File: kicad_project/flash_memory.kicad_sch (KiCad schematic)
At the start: 4 parts, among them U1 W25Q128JVSIQ

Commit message: Pcb to production
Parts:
- removed TP6: VDD_SPI, TestPoint:TestPoint_Pad_D1.0mm, symbol Connector:TestPoint
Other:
- note added: "FLASH MEMORY"
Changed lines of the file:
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@@
 	(title_block
 		(title "WebScreen Project")
-		(rev "0")
+		(date "2024-11-02")
+		(rev "1.2")
 		(company "HW Media Lab LLC")
 	)
@@
 		(color 0 0 0 0)
 	)
-	(junction
-		(at 138.43 95.25)
-		(diameter 0)
-		(color 0 0 0 0)
-	)
 	(wire
 		(pts
@@
 	(wire
 		(pts
-			(xy 138.43 95.25) (xy 152.4 95.25)
-		)
-		(stroke
-			(width 0)
-			(type default)
-		)
-	)
-	(wire
-		(pts
 			(xy 166.37 97.79) (xy 166.37 105.41)
 		)
@@
 	(wire
 		(pts
-			(xy 125.73 95.25) (xy 138.43 95.25)
+			(xy 125.73 95.25) (xy 152.4 95.25)
 		)
 		(stroke
@@
 			(width 0)
 			(type default)
+		)
+	)
+	(text "FLASH MEMORY"
+		(exclude_from_sim no)
+		(at 208.534 28.956 0)
+		(effects
+			(font
+				(face "ISOCPEUR")
+				(size 7.62 7.62)
+				(thickness 0.254)
+				(bold yes)
+			)
+			(justify left bottom)
 		)
 	)
@@
 		(shape output)
 		(at 182.88 113.03 0)
-		(fields_autoplaced yes)
 		(effects
 			(font
@@
 		(shape output)
 		(at 182.88 110.49 0)
-		(fields_autoplaced yes)
 		(effects
 			(font
@@
 		(shape output)
 		(at 182.88 118.11 0)
-		(fields_autoplaced yes)
 		(effects
 			(font
@@
 		(shape output)
 		(at 182.88 97.79 0)
-		(fields_autoplaced yes)
 		(effects
 			(font
@@
 		(shape output)
 		(at 182.88 115.57 0)
-		(fields_autoplaced yes)
 		(effects
 			(font
@@
 		(shape output)
 		(at 182.88 107.95 0)
-		(fields_autoplaced yes)
 		(effects
 			(font
@@
 		(shape output)
 		(at 182.88 105.41 0)
-		(fields_autoplaced yes)
 		(effects
 			(font
@@
 			)
 			(justify left)
-		)
-	)
-	(symbol
-		(lib_id "Connector:TestPoint")
-		(at 138.43 95.25 0)
-		(unit 1)
-		(exclude_from_sim no)
-		(in_bom no)
-		(on_board yes)
-		(dnp yes)
-		(fields_autoplaced yes)
-		(property "Reference" "TP6"
-			(at 139.827 90.7359 0)
-			(effects
-				(font
-					(size 1.27 1.27)
-				)
-				(justify left)
-			)
-		)
-		(property "Value" "VDD_SPI"
-			(at 139.827 93.1601 0)
-			(effects
-				(font
-					(size 1.27 1.27)
-				)
-				(justify left)
-			)
-		)
-		(property "Footprint" "TestPoint:TestPoint_Pad_D1.0mm"
-			(at 143.51 95.25 0)
-			(effects
-				(font
-					(size 1.27 1.27)
-				)
-				(hide yes)
-			)
-		)
-		(property "Datasheet" "~"
-			(at 143.51 95.25 0)
-			(effects
-				(font
-					(size 1.27 1.27)
-				)
-				(hide yes)
-			)
-		)
-		(property "Description" ""
-			(at 138.43 95.25 0)
-			(effects
-				(font
-					(size 1.27 1.27)
-				)
-				(hide yes)
-			)
-		)
-		(property "MFN" ""
-			(at 138.43 95.25 0)
-			(effects
-				(font
-					(size 1.27 1.27)
-				)
-				(hide yes)
-			)
-		)
-		(pin "1"
-		)
-		(instances
-			(project "Display_pcb"
-				(path "/b5a94c04-25f7-450f-b87b-275489bc56c3/8e85ac6e-1427-45a0-aa64-3ffb0278b793"
-					(reference "TP6")
-					(unit 1)
-				)
-			)
 		)
 	)
@@
 			)
 		)
+		(property "Sim.Device" ""
+			(at 152.4 113.03 0)
+			(effects
+				(font
+					(size 1.27 1.27)
+				)
+				(hide yes)
+			)
+		)
+		(property "Sim.Pins" ""
+			(at 152.4 113.03 0)
+			(effects
+				(font
+					(size 1.27 1.27)
+				)
+				(hide yes)
+			)
+		)
 		(pin "1"
 		)
@@
 			)
 		)
+		(property "Sim.Device" ""
+			(at 125.73 100.33 0)
+			(effects
+				(font
+					(size 1.27 1.27)
+				)
+				(hide yes)
+			)
+		)
+		(property "Sim.Pins" ""
+			(at 125.73 100.33 0)
+			(effects
+				(font
+					(size 1.27 1.27)
+				)
+				(hide yes)
+			)
+		)
 		(pin "1"
 		)
@@
 			(at 173.99 97.79 0)
 			(effects
+				(font
+					(size 1.27 1.27)
+				)
+				(hide yes)
+			)
+		)
+		(property "Sim.Device" ""
+			(at 173.99 97.79 0)
+			(effects
+				(font
+					(size 1.27 1.27)
+				)
+				(hide yes)
+			)
+		)
+		(property "Sim.Pins" ""
+			(at 173.99 97.79 0)
+			(effects

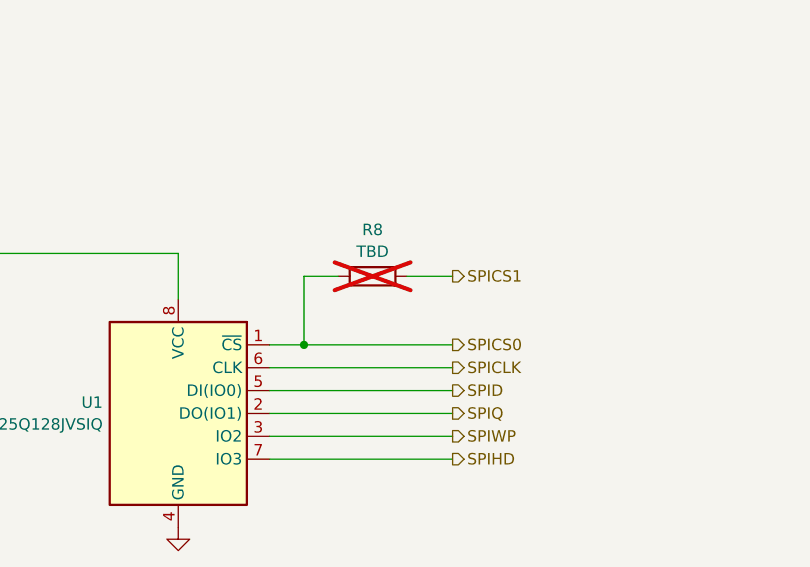
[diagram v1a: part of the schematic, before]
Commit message: Design revision: SD improvements, flash update, silkscreen and USB differential fix
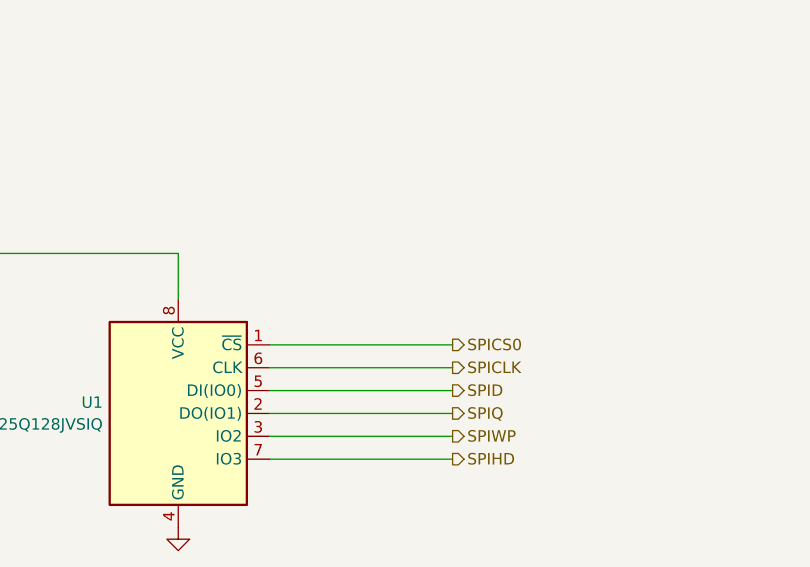
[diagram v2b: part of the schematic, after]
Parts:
- removed R8: TBD, Resistor_SMD:R_0402_1005Metric, symbol Device:R
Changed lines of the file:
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@@
-	)
-	(junction
-		(at 166.37 105.41)
-		(diameter 0)
-		(color 0 0 0 0)
 	)
 	(junction
@@
 	(wire
 		(pts
-			(xy 166.37 105.41) (xy 182.88 105.41)
+			(xy 162.56 105.41) (xy 182.88 105.41)
 		)
 		(stroke
@@
 	(wire
 		(pts
-			(xy 177.8 97.79) (xy 182.88 97.79)
-		)
-		(stroke
-			(width 0)
-			(type default)
-		)
-	)
-	(wire
-		(pts
-			(xy 162.56 105.41) (xy 166.37 105.41)
-		)
-		(stroke
-			(width 0)
-			(type default)
-		)
-	)
-	(wire
-		(pts
-			(xy 166.37 97.79) (xy 166.37 105.41)
-		)
-		(stroke
-			(width 0)
-			(type default)
-		)
-	)
-	(wire
-		(pts
 			(xy 125.73 92.71) (xy 125.73 95.25)
 		)
@@
 		(pts
 			(xy 125.73 95.25) (xy 152.4 95.25)
-		)
-		(stroke
-			(width 0)
-			(type default)
-		)
-	)
-	(wire
-		(pts
-			(xy 170.18 97.79) (xy 166.37 97.79)
 		)
 		(stroke
@@
 		(shape output)
 		(at 182.88 118.11 0)
-		(effects
-			(font
-				(size 1.27 1.27)
-			)
-			(justify left)
-		)
-	)
-	(hierarchical_label "SPICS1"
-		(shape output)
-		(at 182.88 97.79 0)
 		(effects
 			(font
@@
 					(unit 1)
 				)
-			)
-		)
-	)
-	(symbol
-		(lib_id "Device:R")
-		(at 173.99 97.79 90)
-		(unit 1)
-		(exclude_from_sim no)
-		(in_bom no)
-		(on_board yes)
-		(dnp yes)
-		(property "Reference" "R8"
-			(at 173.99 92.6297 90)
-			(effects
-				(font
-					(size 1.27 1.27)
-				)
-			)
-		)
-		(property "Value" "TBD"
-			(at 173.99 95.0539 90)
-			(effects
-				(font
-					(size 1.27 1.27)
-				)
-			)
-		)
-		(property "Footprint" "Resistor_SMD:R_0402_1005Metric"
-			(at 173.99 99.568 90)
-			(effects
-				(font
-					(size 1.27 1.27)
-				)
-				(hide yes)
-			)
-		)
-		(property "Datasheet" "~"
-			(at 173.99 97.79 0)
-			(effects
-				(font
-					(size 1.27 1.27)
-				)
-				(hide yes)
-			)
-		)
-		(property "Description" ""
-			(at 173.99 97.79 0)
-			(effects
-				(font
-					(size 1.27 1.27)
-				)
-				(hide yes)
-			)
-		)
-		(property "MFN" ""
-			(at 173.99 97.79 0)
-			(effects
-				(font
-					(size 1.27 1.27)
-				)
-				(hide yes)
-			)
-		)
-		(property "Sim.Device" ""
-			(at 173.99 97.79 0)
-			(effects
-				(font
-					(size 1.27 1.27)
-				)
-				(hide yes)
-			)
-		)
-		(property "Sim.Pins" ""
-			(at 173.99 97.79 0)
-			(effects
-				(font
-					(size 1.27 1.27)
-				)
-				(hide yes)
-			)
-		)
-		(pin "1"
-		)
-		(pin "2"
-		)
-		(instances
-			(project "Display_pcb"
-				(path "/b5a94c04-25f7-450f-b87b-275489bc56c3/8e85ac6e-1427-45a0-aa64-3ffb0278b793"
-					(reference "R8")
-					(unit 1)
-				)
